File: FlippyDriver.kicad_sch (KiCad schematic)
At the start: 99 parts, among them J1 Data Harness In, J2 Data Harness Out, J3 Board Harness, J5 24V Input, J6 AVR ISCP, J7 24V Input, Q1 AO3401A, Q2 AO3400A, Q47 2N7002, Q48 LBSS84LT1G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

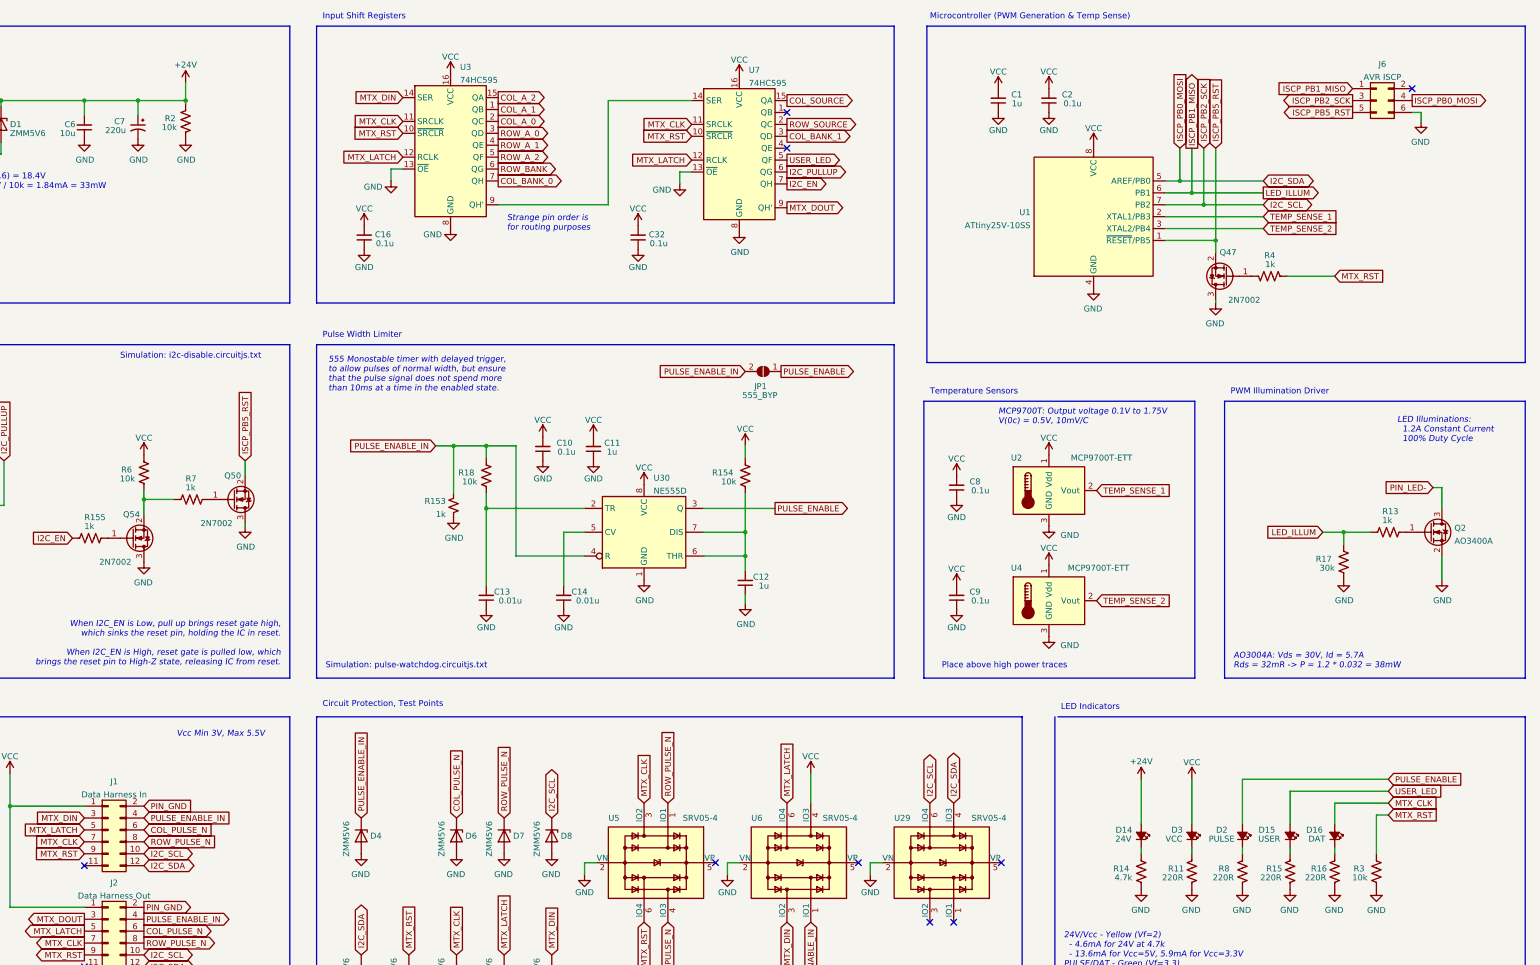
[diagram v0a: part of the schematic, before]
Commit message: Add subrevision, reference submodule objects
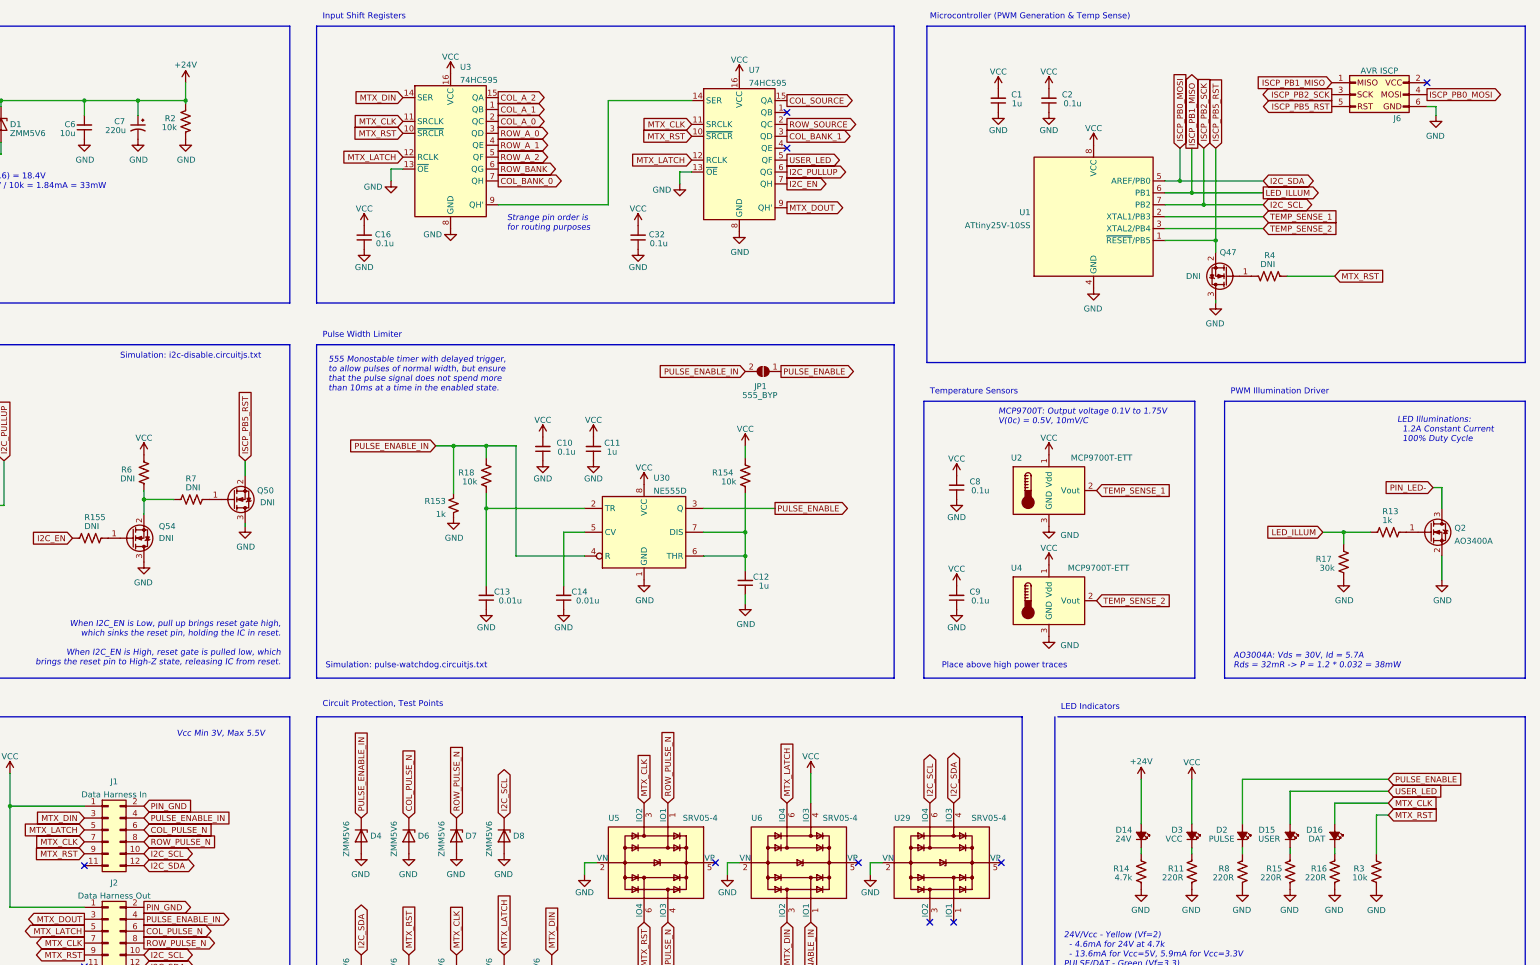
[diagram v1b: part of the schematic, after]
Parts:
- J1, J2: Digikey (none) -> 2057-BHR-12-VUA-ND
- J3: footprint FlippyDriver:Connector_MegaMax_3000 -> Nieto_Connector:Luminator_MAX3000
- J5: Digikey (none) -> 732-5930-ND
- J6: footprint FlippyDriver:ICSP-PogoPads -> Nieto_Connector:ICSP-PogoPads; symbol Connector_Generic:Conn_02x03_Odd_Even -> Nieto_Connector:ISCP
- J7: Digikey (none) -> 732-10955-ND
- Q47, Q50, Q54: value 2N7002 -> DNI; LCSC C8545 -> (none)
- R155, R4, R7: value 1k -> DNI; LCSC C21190 -> (none)
- R6: value 10k -> DNI; LCSC C25804 -> (none)
- TP6: Digikey (none) -> 36-5006-ND
- U1: Digikey (none) -> 556-ATTINY13A-SSUR
- U3, U7: LCSC C5947 -> C5947
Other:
- moved on the sheet: D6, D7, D8

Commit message: Initial draft of Revision D
- Remove I2C Bus, and replace with PWM Input
- Remove temp sensors due to no I2C bus
- Add 5V aux output from 24V, supports LM7805 (w/ Heatsink) and VX7805
- Larger components for high current nets
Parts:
- removed C1: 1u, Capacitor_SMD:C_0603_1608Metric, symbol Device:C_Small
- removed C2, C8, C9: 0.1u, Capacitor_SMD:C_0603_1608Metric, symbol Device:C_Small
- removed D8: ZMM5V6, Diode_SMD:D_MiniMELF, symbol Diode:ZMMxx
- removed J6: AVR ISCP, Nieto_Connector:ICSP-PogoPads, symbol Nieto_Connector:ISCP
- removed Q1: AO3401A, Package_TO_SOT_SMD:SOT-23, symbol Transistor_FET:AO3401A
- removed Q2: AO3400A, Package_TO_SOT_SMD:SOT-23, symbol Transistor_FET:AO3400A
- removed Q47, Q50, Q54: DNI, Package_TO_SOT_SMD:SOT-23, symbol Transistor_FET:2N7002
- removed Q48, Q49, Q52, Q53: LBSS84LT1G, Package_TO_SOT_SMD:SOT-23, symbol Device:Q_PMOS_GSD
- removed Q51: 2N7002, Package_TO_SOT_SMD:SOT-23, symbol Transistor_FET:2N7002
- removed R10, R12: 4.7k, Resistor_SMD:R_0603_1608Metric, symbol Device:R_US
- removed R155, R6, R7: DNI, Resistor_SMD:R_0603_1608Metric, symbol Device:R_US
- removed R9: 1k, Resistor_SMD:R_0603_1608Metric, symbol Device:R_US
- removed TP9: SDA, TestPoint:TestPoint_Pad_D1.5mm, symbol Connector:TestPoint
- removed U1: ATtiny25V-10SS, Package_SO:SOIC-8W_5.3x5.3mm_P1.27mm, symbol MCU_Microchip_ATtiny:ATtiny25V-10S
- removed U2, U4: MCP9700T-ETT, Package_TO_SOT_SMD:SOT-23, symbol Sensor_Temperature:MCP9700T-ETT
- removed U29: SRV05-4, Package_TO_SOT_SMD:SOT-23-6, symbol Power_Protection:SRV05-4
- added C15, C17: 10u, Capacitor_SMD:C_0805_2012Metric, symbol Device:C_Small
- added Q1: VBJ2456, Package_TO_SOT_SMD:SOT-223-3_TabPin2, symbol Device:Q_PMOS_GDSD
- added Q2: BSP110, Package_TO_SOT_SMD:SOT-223-3_TabPin2, symbol Device:Q_NMOS_GDSD
- added U31: VX7805-500, Converter_DCDC:Converter_DCDC_RECOM_R-78E-0.5_THT, symbol Regulator_Linear:L7805
- R1, R2: footprint Resistor_SMD:R_0603_1608Metric -> Resistor_SMD:R_0805_2012Metric; Digikey RMCF0603JT10K0CT-ND -> RMCF0805JT10K0CT-ND; LCSC C25804 -> C17414
- R14: value 4.7k -> 10k; footprint Resistor_SMD:R_1206_3216Metric -> Resistor_SMD:R_0805_2012Metric; Digikey RMCF1206JT4K70CT-ND -> RMCF0805JT10K0CT-ND; LCSC C17936 -> C17414
- R4: value DNI -> 10k; Digikey RNCP0603FTD1K00CT-ND -> RMCF0603JT10K0CT-ND; LCSC (none) -> C25804
- TP10: value SCL -> LED
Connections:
- net ISCP_PB1_MISO is gone; now on net LED_ILLUM: R13.2, R17.2
- net +24V: now also C15.2, Q1.3 (S), U31.1 (IN)
- net COL_PULSE_N: now also U5.1 (IO1); no longer U5.4 (IO3)
- net GND: now also J1.12 (Pin_12), C15.1, C17.1, Q2.3 (S), U31.2 (GND)
- net MTX_CLK: now also U6.3 (IO2); no longer U5.3 (IO2)
- net MTX_DIN: now also U5.3 (IO2); no longer U6.3 (IO2)
- net MTX_LATCH: now also U5.6 (IO4); no longer U6.6 (IO4)
- net MTX_RST: now also U6.6 (IO4); no longer R4.2, U5.6 (IO4)
- net PIN_LED-: now also Q2.2 (D), Q2.4 (D)
- net PULSE_ENABLE_IN: now also U5.4 (IO3); no longer U6.1 (IO1)
- net ROW_PULSE_N: now also U6.4 (IO3); no longer U5.1 (IO1)
- net VCC: now also R4.2; no longer U6.4 (IO3)
- net at F1.2, JP2.2 (B): now also Q1.2 (D), Q1.4 (D)
- net 5V_OUT: now reaches J1.11 (Pin_11)
- net 5V_OUT: now also C17.2, U31.3 (OUT)
- net at R5.1: now also U6.5 (VP)
- net at R4.1: now also U5.5 (VP)
- net at D1.2 (A), R1.2: now also Q1.1 (G)
- net at R13.1: now also Q2.1 (G)
- net I2C_EN: no longer names the net of U7.7 (QH)
- net I2C_PULLUP: no longer names the net of U7.6 (QG)
- net I2C_SCL renamed LED_ILLUM
- net LED_ILLUM: now also D9.1 (K), U6.1 (IO1)
- removed net I2C_SDA: D9.1 (K), J1.12 (Pin_12), J2.12 (Pin_12)
- no-connect marks 11 -> 7
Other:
- note added: "Aux 5V output"
- note added: "Input Shift Registers & LEDs"
- note removed: "I2C Bus with switches to allow only a chain of boards with one set of pullups"
- note removed: "I2C Pull-ups and Reset"
- note removed: "Input Shift Registers"
- note removed: "LED Indicators"
- note removed: "MCP9700T: Output voltage 0.1V to 1.75V V(0c) = 0.5V, 10mV/C"
- note removed: "Microcontroller (PWM Generation & Temp Sense)"
- note removed: "Place above high power traces"
- note removed: "Simulation: i2c-disable.circuitjs.txt"
- note removed: "Temperature Sensors"
- note removed: "When I2C_EN is Low, pull up brings reset gate high, which sinks the reset pin, holding the IC in reset. When I2C_EN is High, reset gate is pulled low, which brings the reset pin to High-Z state, releasing IC from reset."
- moved on the sheet: C10, C11, C12, C13, C14, C3, C4, C5, C6, C7, D1, D10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

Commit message: Finalize Revision D
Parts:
- added F2: 500mA, Fuse:Fuse_0603_1608Metric, symbol Device:Polyfuse
- added JP3: FUSE_BYP, Jumper:SolderJumper-2_P1.3mm_Open_RoundedPad1.0x1.5mm, symbol Jumper:SolderJumper_2_Open
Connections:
- net VCC: now also F2.1, JP3.1 (A); no longer J1.1 (Pin_1), J2.1 (Pin_1)
- new net: F2.2, J1.1 (Pin_1), J2.1 (Pin_1), JP3.2 (B)
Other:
- moved on the sheet: C10, C11, C12, C13, C14, JP1, R13, R153, R154, R17, R18, TP4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

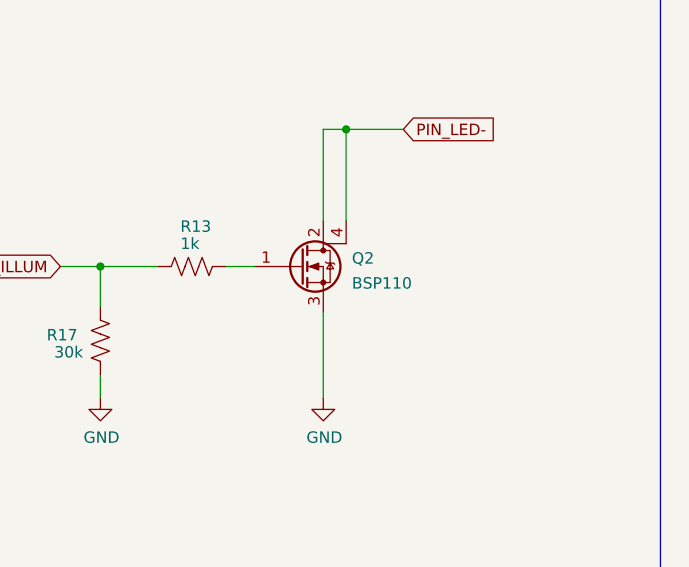
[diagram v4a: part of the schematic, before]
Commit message: Replace out of stock parts with current JLCPCB parts
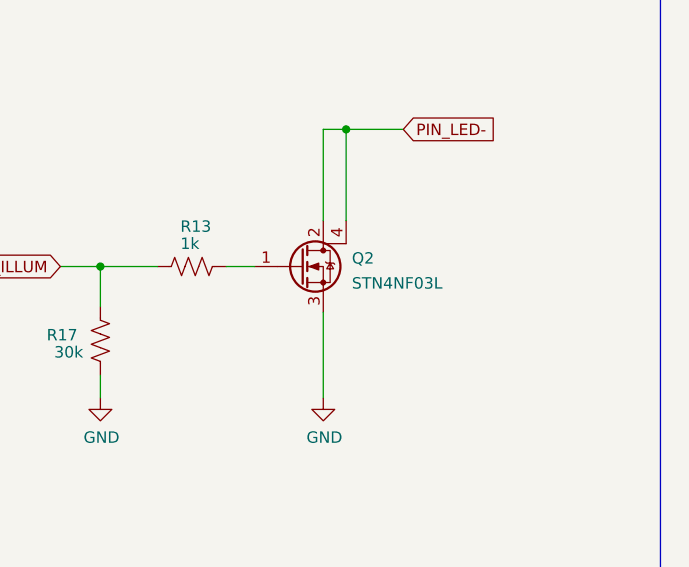
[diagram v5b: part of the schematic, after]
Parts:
- Q2: value BSP110 -> STN4NF03L; Digikey IRFL024ZTRPBFCT-ND -> 497-4525-1-ND; LCSC C724993 -> C85568
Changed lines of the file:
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@@
   (title_block
     (title "Luminator MAX3000 Custom Driver Board")
-    (date "2022-08-30")
-    (rev "D")
+    (date "2022-12-01")
+    (rev "D.1")
   )
   (junction (at 59.055 48.895) (diameter 0) (color 0 0 0 0)
@@
       (effects (font (size 1.27 1.27)) (justify left))
     )
-    (property "Value" "BSP110" (id 1) (at 377.19 185.3816 0)
+    (property "Value" "STN4NF03L" (id 1) (at 377.19 185.3816 0)
       (effects (font (size 1.27 1.27)) (justify left))
     )
@@
       (effects (font (size 1.27 1.27)) hide)
     )
-    (property "LCSC" "C724993" (id 4) (at 371.475 183.515 0)
+    (property "LCSC" "C85568" (id 4) (at 371.475 183.515 0)
       (effects (font (size 1.27 1.27)) hide)
     )
-    (property "Digikey" " IRFL024ZTRPBFCT-ND" (id 5) (at 371.475 183.515 0)
+    (property "Digikey" "497-4525-1-ND" (id 5) (at 371.475 183.515 0)
       (effects (font (size 1.27 1.27)) hide)
     )
@@
     )
     (path "/d107bce9-58f1-4bfc-aeb8-38d5741a45b2"
-      (reference "Q2") (unit 1) (value "BSP110") (footprint "Package_TO_SOT_SMD:SOT-223-3_TabPin2")
+      (reference "Q2") (unit 1) (value "STN4NF03L") (footprint "Package_TO_SOT_SMD:SOT-223-3_TabPin2")
     )
     (path "/00000000-0000-0000-0000-00005fec42d4/fc9667d1-d03a-4d32-a6d7-bacd0ead3170"

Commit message: Replace LCSC parts with ones in stock
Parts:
- Q2: value STN4NF03L -> FDT439N; Digikey 497-4525-1-ND -> FDT439NCT-ND; LCSC C85568 -> C467785
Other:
- note added: "VBJ2456: Vds = 35V, Vgsmax = +/- 20V At 4A / 4.5Vgs -> Rds = 55mR -> P = 180mW"
- note removed: "AO3401A: Vds = 30V, Vgsmax = +/- 12V At 3A / 5.6Vgs -> Rds = 60mR -> P = 180mW"
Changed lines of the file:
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@@
     (effects (font (size 1.27 1.27)) (justify left bottom))
   )
-  (text "AO3401A: Vds = 30V, Vgsmax = +/- 12V\nAt 3A / 5.6Vgs -> Rds = 60mR -> P = 180mW"
+  (text "VBJ2456: Vds = 35V, Vgsmax = +/- 20V\nAt 4A / 4.5Vgs -> Rds = 55mR -> P = 180mW"
     (at 20.955 24.765 0)
     (effects (font (size 1.27 1.27) italic) (justify left bottom))
@@
       (effects (font (size 1.27 1.27)) (justify left))
     )
-    (property "Value" "STN4NF03L" (id 1) (at 377.19 185.3816 0)
+    (property "Value" "FDT439N" (id 1) (at 377.19 185.3816 0)
       (effects (font (size 1.27 1.27)) (justify left))
     )
@@
       (effects (font (size 1.27 1.27)) hide)
     )
-    (property "LCSC" "C85568" (id 4) (at 371.475 183.515 0)
+    (property "LCSC" "C467785" (id 4) (at 371.475 183.515 0)
       (effects (font (size 1.27 1.27)) hide)
     )
-    (property "Digikey" "497-4525-1-ND" (id 5) (at 371.475 183.515 0)
+    (property "Digikey" "FDT439NCT-ND" (id 5) (at 371.475 183.515 0)
       (effects (font (size 1.27 1.27)) hide)
     )
@@
     )
     (path "/d107bce9-58f1-4bfc-aeb8-38d5741a45b2"
-      (reference "Q2") (unit 1) (value "STN4NF03L") (footprint "Package_TO_SOT_SMD:SOT-223-3_TabPin2")
+      (reference "Q2") (unit 1) (value "FDT439N") (footprint "Package_TO_SOT_SMD:SOT-223-3_TabPin2")
     )
     (path "/00000000-0000-0000-0000-00005fec42d4/fc9667d1-d03a-4d32-a6d7-bacd0ead3170"

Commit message: Revision E, adds voltage bounding and thermal protection
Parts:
- removed C10, C16, C32, C5: 0.1u, Capacitor_SMD:C_0603_1608Metric, symbol Device:C_Small
- removed C11, C12, C4: 1u, Capacitor_SMD:C_0603_1608Metric, symbol Device:C_Small
- removed C13, C14: 0.01u, Capacitor_SMD:C_0603_1608Metric, symbol Device:C_Small
- removed C15, C17, C3, C6: 10u, Capacitor_SMD:C_0805_2012Metric, symbol Device:C_Small
- removed C7: 220u, Capacitor_SMD:CP_Elec_10x10, symbol Device:C_Polarized_Small_US
- removed D1, D10, D11, D12, D13, D4, D6, D7, D9: ZMM5V6, Diode_SMD:D_MiniMELF, symbol Diode:ZMMxx
- removed D14, D3: 19-213/Y2C-CQ2R2L/3T(CY), LED_SMD:LED_0603_1608Metric, symbol Device:LED_Small_Filled
- removed D15: 19-217/BHC-ZL1M2RY/3T, LED_SMD:LED_0603_1608Metric, symbol Device:LED_Small_Filled
- removed D16, D2: 19-217/GHC-YR1S2/3T, LED_SMD:LED_0603_1608Metric, symbol Device:LED_Small_Filled
- removed F1: 5A, Fuse:Fuse_0603_1608Metric, symbol Device:Polyfuse
- removed F2: 500mA, Fuse:Fuse_0603_1608Metric, symbol Device:Polyfuse
- removed H1, H2, H3, H4: MountingHole_Pad, MountingHole:MountingHole_3.5mm_Pad_TopBottom, symbol Mechanical:MountingHole_Pad
- removed H5: MountingHole_Pad, MountingHole:MountingHole_4.5mm_Pad_TopBottom, symbol Mechanical:MountingHole_Pad
- removed J1: Data Harness In, Connector_IDC:IDC-Header_2x06_P2.54mm_Vertical, symbol Connector_Generic:Conn_02x06_Odd_Even
- removed J2: Data Harness Out, Connector_IDC:IDC-Header_2x06_P2.54mm_Vertical, symbol Connector_Generic:Conn_02x06_Odd_Even
- removed J3: Board Harness, Nieto_Connector:Luminator_MAX3000, symbol Connector_Generic:Conn_02x32_Odd_Even
- removed J5: 24V Input, Connector_BarrelJack:BarrelJack_Horizontal, symbol Connector:Barrel_Jack_MountingPin
- removed J7: 24V Input, TerminalBlock_Phoenix:TerminalBlock_Phoenix_MKDS-1,5-2_1x02_P5.00mm_Horizontal, symbol Connector:Screw_Terminal_01x02
- removed JP1: 555_BYP, Jumper:SolderJumper-2_P1.3mm_Open_RoundedPad1.0x1.5mm, symbol Jumper:SolderJumper_2_Open
- removed JP2, JP3: FUSE_BYP, Jumper:SolderJumper-2_P1.3mm_Open_RoundedPad1.0x1.5mm, symbol Jumper:SolderJumper_2_Open
- removed Q1: VBJ2456, Package_TO_SOT_SMD:SOT-223-3_TabPin2, symbol Device:Q_PMOS_GDSD
- removed Q2: FDT439N, Package_TO_SOT_SMD:SOT-223-3_TabPin2, symbol Device:Q_NMOS_GDSD
- removed R1, R14, R2: 10k, Resistor_SMD:R_0805_2012Metric, symbol Device:R_US
- removed R11, R15, R16, R8: 220R, Resistor_SMD:R_0603_1608Metric, symbol Device:R_US
- removed R13: 1k, Resistor_SMD:R_0603_1608Metric, symbol Device:R_US
- removed R153: 1k, Resistor_SMD:R_0603_1608Metric, symbol Device:R_Small_US
- removed R154, R18, R3, R4, R5: 10k, Resistor_SMD:R_0603_1608Metric, symbol Device:R_US
- removed R17: 30k, Resistor_SMD:R_0603_1608Metric, symbol Device:R_US
- removed TP1: CLK, TestPoint:TestPoint_Pad_D1.5mm, symbol Connector:TestPoint
- removed TP10: LED, TestPoint:TestPoint_Pad_D1.5mm, symbol Connector:TestPoint
- removed TP11: DIN, TestPoint:TestPoint_Pad_D1.5mm, symbol Connector:TestPoint
- removed TP12: LAT, TestPoint:TestPoint_Pad_D1.5mm, symbol Connector:TestPoint
- removed TP13: EN, TestPoint:TestPoint_Pad_D1.5mm, symbol Connector:TestPoint
- removed TP14: ROW, TestPoint:TestPoint_Pad_D1.5mm, symbol Connector:TestPoint
- removed TP15: COL, TestPoint:TestPoint_Pad_D1.5mm, symbol Connector:TestPoint
- removed TP2: RST, TestPoint:TestPoint_Pad_D1.5mm, symbol Connector:TestPoint
- removed TP3: DOUT, TestPoint:TestPoint_Pad_D1.5mm, symbol Connector:TestPoint
- removed TP4: VCC, TestPoint:TestPoint_Pad_D1.5mm, symbol Connector:TestPoint
- removed TP5: GND, TestPoint:TestPoint_Pad_D1.5mm, symbol Connector:TestPoint
- removed TP6: GND, TestPoint:TestPoint_Keystone_5005-5009_Compact, symbol Connector:TestPoint
- removed TP7: EN_IN, TestPoint:TestPoint_Pad_D1.5mm, symbol Connector:TestPoint
- removed U3, U7: 74HC595, Package_SO:SOIC-16_3.9x9.9mm_P1.27mm, symbol 74xx:74HC595
- removed U30: NE555D, Package_SO:SOIC-8_3.9x4.9mm_P1.27mm, symbol Timer:NE555D
- removed U31: VX7805-500, Converter_DCDC:Converter_DCDC_RECOM_R-78E-0.5_THT, symbol Regulator_Linear:L7805
- removed U5, U6: SRV05-4, Package_TO_SOT_SMD:SOT-23-6, symbol Power_Protection:SRV05-4
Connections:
- no-connect marks 7 -> 0
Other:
- added sheet 5V Output Regulator (5V_Reg.kicad_sch)
- added sheet Board Harnesses (BoardHarnesses.kicad_sch)
- added sheet Indicator LEDs (Indicators.kicad_sch)
- added sheet Power Input and Protection (PowerInput.kicad_sch)
- added sheet Pulse Protection (PulseProtection.kicad_sch)
- added sheet Shift Registers (ShiftRegisters.kicad_sch)
- added sheet Testpoints (Testpoints.kicad_sch)
- note removed: "(24-5.6) = 18.4V 18.4V / 10k = 1.84mA = 33mW"
- note removed: "24V/Vcc - Yellow (Vf=2) - 4.6mA for 24V at 4.7k - 13.6mA for Vcc=5V, 5.9mA for Vcc=3.3V PULSE/DAT - Green (Vf=3.3) - 7.7mA for Vcc=5V, <1mA for Vcc=3.3V USER - Blue (Vf=2.8) - 10mA for Vcc=5V, 2.2mA for Vcc=3.3V"
- note removed: "555 Monostable timer with delayed trigger, to allow pulses of normal width, but ensure that the pulse signal does not spend more than 10ms at a time in the enabled state."
- note removed: "<-- Towards Edge Towards Dots -->"
- note removed: "AO3004A: Vds = 30V, Id = 5.7A Rds = 32mR -> P = 1.2 * 0.032 = 38mW"
- note removed: "Aux 5V output"
- note removed: "Board Harnesses"
- note removed: "Circuit Protection, Test Points"
- note removed: "Input Power"
- note removed: "Input Shift Registers & LEDs"
- note removed: "LED Illuminations: 1.2A Constant Current 100% Duty Cycle"
- note removed: "PWM Illumination Driver"
- note removed: "Pulse Width Limiter"
- note removed: "Simulation: pulse-watchdog.circuitjs.txt"
- note removed: "Strange pin order is for routing purposes"
- note removed: "VBJ2456: Vds = 35V, Vgsmax = +/- 20V At 4A / 4.5Vgs -> Rds = 55mR -> P = 180mW"
- note removed: "Vcc Min 3V, Max 5.5V"
